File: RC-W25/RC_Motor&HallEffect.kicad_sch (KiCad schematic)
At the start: 11 parts, among them P2 JST CONN, Q1 NMOS, SW2 Button, U4 TMAG5253, U5 TMAG5253

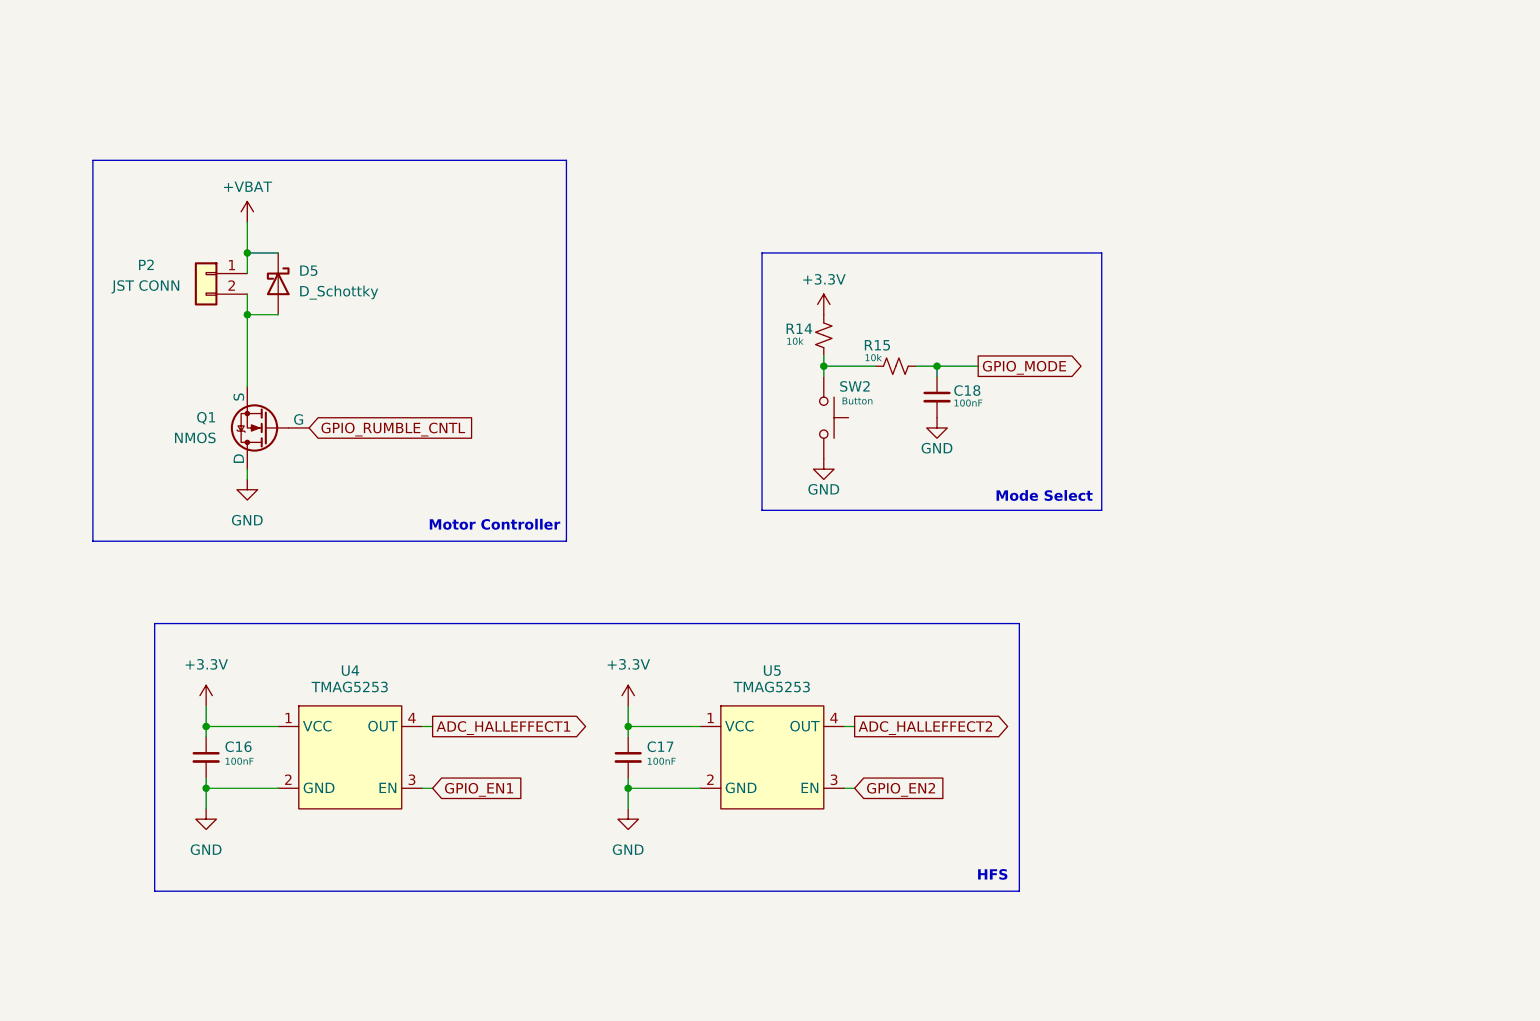
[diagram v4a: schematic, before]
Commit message: Began Routing
Only need to spec out buttons before completion
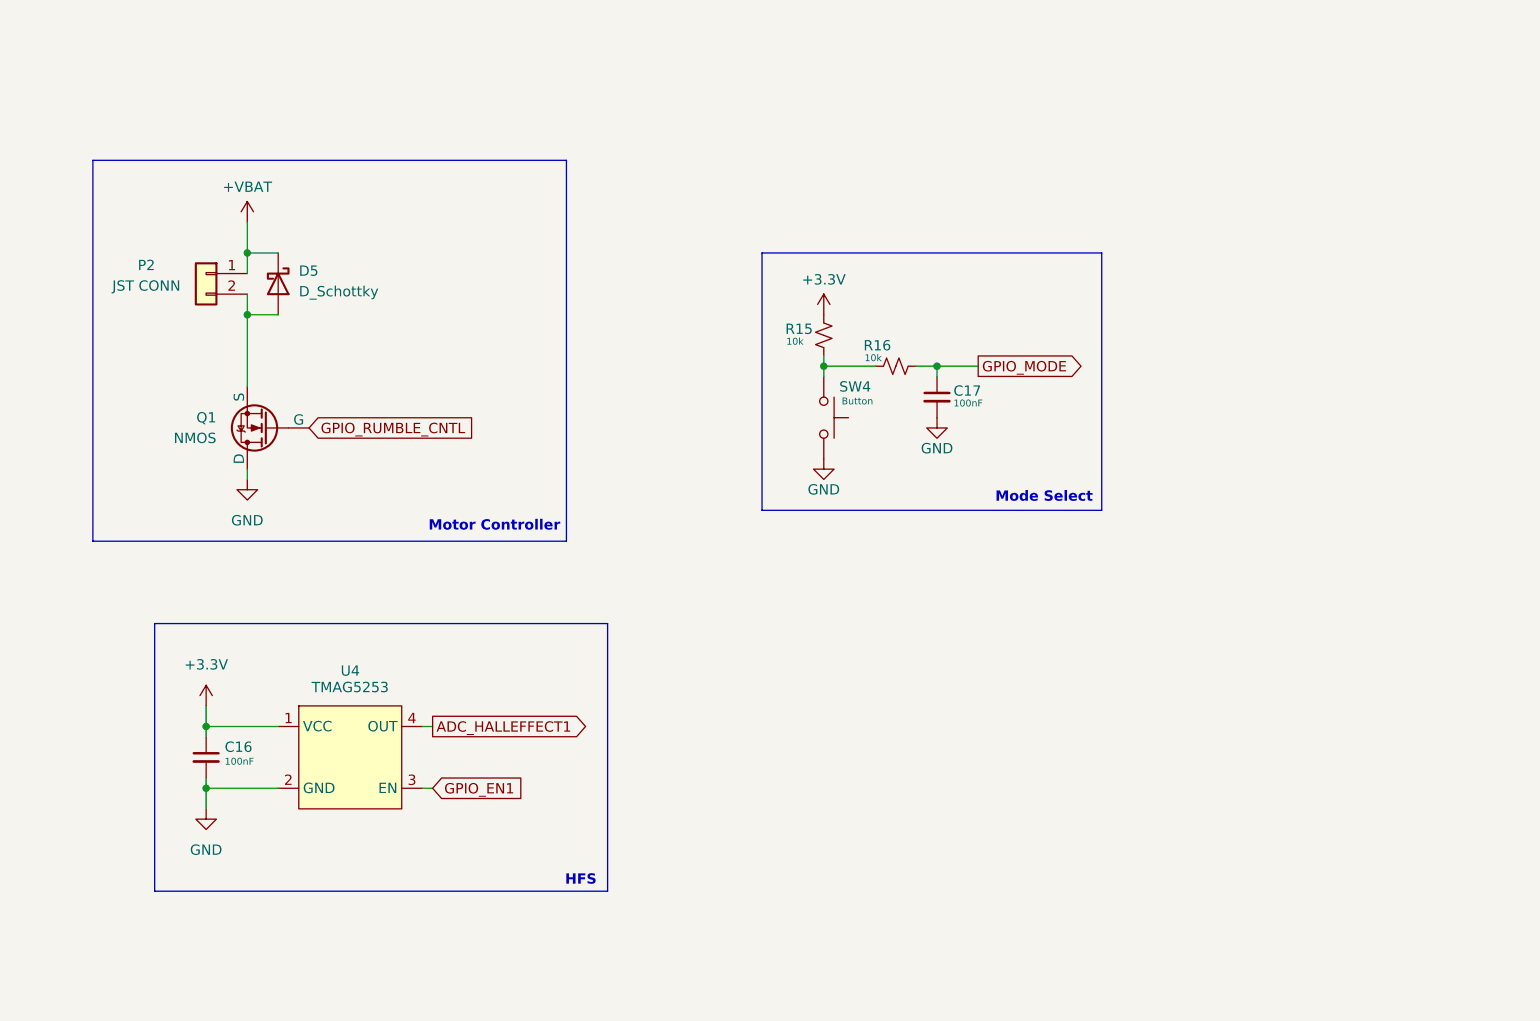
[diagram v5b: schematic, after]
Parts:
- removed C17: 100nF, Capacitor_SMD:C_0402_1005Metric, symbol Device:C_Small
- removed U5: TMAG5253, Library:X2SON4_DMR_TEX-M, symbol New_Library_0:TMAG5253_Linear_Hall_Effect_Sensor
- Q1: footprint Sensor:SOT-23_2P9X1P3_DIO -> Package_TO_SOT_SMD:SOT-23; LCSC# (none) -> C443825
- U4: footprint Library:X2SON4_DMR_TEX-M -> footprints:X2SON4_DMR_TEX
- renumbered C18 to C17, R14 to R15, R15 to R16, SW2 to SW4

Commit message: EM Custom RC V1
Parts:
- SW4: footprint (none) -> footprints:SW-SMD_L3.9-W3.0-P4.45; LCSC# (none) -> C720477
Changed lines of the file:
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@@
 			)
 		)
-		(property "Footprint" ""
+		(property "Footprint" "footprints:SW-SMD_L3.9-W3.0-P4.45"
 			(at 157.48 77.47 0)
 			(effects
@@
 			)
 		)
-		(property "Datasheet" "~"
+		(property "Datasheet" "https://www.lcsc.com/datasheet/lcsc_datasheet_2409302330_XUNPU-TS-1088-AR02016_C720477.pdf"
 			(at 157.48 77.47 0)
 			(effects
@@
 			)
 		)
-		(property "LCSC#" ""
+		(property "LCSC#" "C720477"
 			(at 152.4 77.47 0)
 			(effects

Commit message: crc v1
finalized!! finally!! yes!!

- spec out 3.7V 1000mAh cell
- spec out ultra-thin coin motor

^make sure they have a jst-ph male connector or are organized to be ordered alongside one for manual soldering.
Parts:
- P2: footprint Library:CONN02_502352_MOL -> footprints:CONN-SMD_2P-P2.00_XUNPU_WAFER-PH2.0-2PWB; LCSC# (none) -> C3029440
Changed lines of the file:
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@@
 			)
 		)
-		(property "Footprint" "Library:CONN02_502352_MOL"
+		(property "Footprint" "footprints:CONN-SMD_2P-P2.00_XUNPU_WAFER-PH2.0-2PWB"
 			(at 76.2 59.69 0)
 			(effects
@@
 			)
 		)
-		(property "Datasheet" "~"
+		(property "Datasheet" "https://www.lcsc.com/datasheet/lcsc_datasheet_2411192313_XUNPU-WAFER-PH2-0-2PWB_C3029440.pdf"
 			(at 76.2 59.69 0)
 			(effects
@@
 			)
 		)
-		(property "LCSC#" ""
+		(property "LCSC#" "C3029440"
 			(at 76.2 59.69 0)
 			(effects

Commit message: crc v1
quick fixes
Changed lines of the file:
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@@
 	)
 	(symbol
-		(lib_id "power:GND")
+		(lib_id "power:Earth")
 		(at 166.37 77.47 0)
 		(unit 1)
@@
 			)
 		)
-		(property "Datasheet" ""
+		(property "Datasheet" "~"
 			(at 166.37 77.47 0)
 			(effects
@@
 			)
 		)
-		(property "Description" "Power symbol creates a global label with name \"GND\" , ground"
+		(property "Description" "Power symbol creates a global label with name \"Earth\""
 			(at 166.37 77.47 0)
 			(effects
@@
 	)
 	(symbol
-		(lib_id "power:GND")
+		(lib_id "power:Earth")
 		(at 152.4 82.55 0)
 		(unit 1)
@@
 			)
 		)
-		(property "Datasheet" ""
+		(property "Datasheet" "~"
 			(at 152.4 82.55 0)
 			(effects
@@
 			)
 		)
-		(property "Description" "Power symbol creates a global label with name \"GND\" , ground"
+		(property "Description" "Power symbol creates a global label with name \"Earth\""
 			(at 152.4 82.55 0)
 			(effects
@@
 	)
 	(symbol
-		(lib_id "power:GND")
+		(lib_id "power:Earth")
 		(at 76.2 125.73 0)
 		(unit 1)
@@
 		)
 		(property "Value" "GND"
-			(at 76.2 130.81 0)
-			(effects
-				(font
-					(size 1.27 1.27)
-				)
+			(at 78.74 126.9999 0)
+			(effects
+				(font
+					(size 1.27 1.27)
+				)
+				(justify left)
 			)
 		)
@@
 			)
 		)
-		(property "Datasheet" ""
+		(property "Datasheet" "~"
 			(at 76.2 125.73 0)
 			(effects
@@
 			)
 		)
-		(property "Description" "Power symbol creates a global label with name \"GND\" , ground"
+		(property "Description" "Power symbol creates a global label with name \"Earth\""
 			(at 76.2 125.73 0)
 			(effects
@@
 	)
 	(symbol
-		(lib_id "power:GND")
+		(lib_id "power:Earth")
 		(at 81.28 85.09 0)
 		(unit 1)
@@
 		)
 		(property "Value" "GND"
-			(at 81.28 90.17 0)
-			(effects
-				(font
-					(size 1.27 1.27)
-				)
+			(at 83.82 86.3599 0)
+			(effects
+				(font
+					(size 1.27 1.27)
+				)
+				(justify left)
 			)
 		)
@@
 			)
 		)
-		(property "Datasheet" ""
+		(property "Datasheet" "~"
 			(at 81.28 85.09 0)
 			(effects
@@
 			)
 		)
-		(property "Description" "Power symbol creates a global label with name \"GND\" , ground"
+		(property "Description" "Power symbol creates a global label with name \"Earth\""
 			(at 81.28 85.09 0)
 			(effects
